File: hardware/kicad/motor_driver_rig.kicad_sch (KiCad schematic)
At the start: 8 parts, among them M1 NEMA-17 stepper motor, M2 NEMA-17 stepper motor, M3 NEMA-17 stepper motor, U1 Arduino Uno + CNC Shield V3

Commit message: schematics: name controller pins the way the boards name them
The three KiCad schematics labelled every controller pin by its MCU function
or STM32 port -- SCK, MISO, I2S_CLK, LED_DIN, PB0 -- which is not what any of
these boards is silkscreened with and not what you plug a wire into. Someone
holding an UNO Q and the schematic had no way to find "I2S_CLK".

Pins now carry the board's own header labels: D13/D12/D11/D8/D9/SCL/D10/A4/D3
on the UNO Q, D0-D10 on the XIAO, D2-D8 on the Uno under the CNC shield. The
signal's role moves into the net label, where it was already half-living
(SPI_SCK_D13, MIC_SD_A4), so each sensor stub still says both what the line
carries and which header pin it lands on. Sensor and driver symbols keep
their datasheet names -- those breakouts really are marked SCK/SDO/STEP.

Two labels were also just wrong, not merely inconvenient: the ring's DIN read
LED_DIN_PB0 when PB0 is header pin D3, and the mic's three lines read
PB10/PB9/PC1 with no header pin at all -- they are SCL, D10 and A4. Mapping is
the board's own gpio-map (arduino_r3_connector.dtsi) for the UNO Q and
board_pins.h for the XIAO; the mic's bit clock is genuinely the odd one out,
since PB10 comes out as the dedicated SCL pin rather than a D-number.

Appendix B.1's table gains the same treatment, and the report PNGs are
re-cropped to the drawing rather than the sheet -- they were carrying about
half a page of blank paper each, which shrank the schematic on the page. The
crop is now derived in the README instead of living in shell history.

Co-Authored-By: Claude Opus 5 <noreply@anthropic.com>
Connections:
- net EN renamed ENABLE_D8
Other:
- note added: "Arduino Uno + CNC Shield V3, one driver socket per motor axis. Shared ~ENABLE line on D8, active-LOW. Uno pins named by header number."
- note removed: "Arduino Uno + CNC Shield V3, one driver socket per motor axis. Shared ~ENABLE line, active-LOW."
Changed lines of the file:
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@@
 		(stroke (width 0) (type default))
 	)
-	(label "EN"
+	(label "ENABLE_D8"
 		(at 94.29 77.775 0)
 		(effects (font (size 1.27 1.27)) (justify left))
@@
 		(effects (font (size 1.27 1.27)) (justify right))
 	)
-	(label "EN"
+	(label "ENABLE_D8"
 		(at 147.06 73.175 0)
 		(effects (font (size 1.27 1.27)) (justify right))
@@
 		(effects (font (size 1.27 1.27)) (justify right))
 	)
-	(label "EN"
+	(label "ENABLE_D8"
 		(at 147.06 128.175 0)
 		(effects (font (size 1.27 1.27)) (justify right))
@@
 		(effects (font (size 1.27 1.27)) (justify right))
 	)
-	(label "EN"
+	(label "ENABLE_D8"
 		(at 147.06 183.175 0)
 		(effects (font (size 1.27 1.27)) (justify right))
@@
 		(effects (font (size 3.0 3.0)) (justify left))
 	)
-	(text "Arduino Uno + CNC Shield V3, one driver socket per motor axis. Shared ~ENABLE line, active-LOW."
+	(text "Arduino Uno + CNC Shield V3, one driver socket per motor axis. Shared ~ENABLE line on D8, active-LOW. Uno pins named by header number."
 		(exclude_from_sim no)
 		(at 20 32 0)
@@
 		(instances
 			(project "epm"
-				(path "/50f33c9c-fe69-4cc4-b722-142f8d680243"
+				(path "/2d634057-a69e-4741-94ac-d6e266f9f302"
 					(reference "U1")
 					(unit 1)
@@
 		(on_board yes)
 		(dnp no)
-		(property "Reference" "#PWR58db"
+		(property "Reference" "#PWRcf7e"
 			(at 94.29 118.41499999999999 0)
 			(effects (font (size 1.27 1.27)) (hide yes))
@@
 		(instances
 			(project "epm"
-				(path "/50f33c9c-fe69-4cc4-b722-142f8d680243"
-					(reference "#PWR58db")
+				(path "/2d634057-a69e-4741-94ac-d6e266f9f302"
+					(reference "#PWRcf7e")
 					(unit 1)
 				)
@@
 		(instances
 			(project "epm"
-				(path "/50f33c9c-fe69-4cc4-b722-142f8d680243"
+				(path "/2d634057-a69e-4741-94ac-d6e266f9f302"
 					(reference "A1")
 					(unit 1)
@@
 		(on_board yes)
 		(dnp no)
-		(property "Reference" "#PWR8cc8"
+		(property "Reference" "#PWRf5da"
 			(at 147.06 75.715 0)
 			(effects (font (size 1.27 1.27)) (hide yes))
@@
 		(instances
 			(project "epm"
-				(path "/50f33c9c-fe69-4cc4-b722-142f8d680243"
-					(reference "#PWR8cc8")
+				(path "/2d634057-a69e-4741-94ac-d6e266f9f302"
+					(reference "#PWRf5da")
 					(unit 1)
 				)
@@
 		(instances
 			(project "epm"
-				(path "/50f33c9c-fe69-4cc4-b722-142f8d680243"
+				(path "/2d634057-a69e-4741-94ac-d6e266f9f302"
 					(reference "M1")
 					(unit 1)
@@
 		(instances
 			(project "epm"
-				(path "/50f33c9c-fe69-4cc4-b722-142f8d680243"
+				(path "/2d634057-a69e-4741-94ac-d6e266f9f302"
 					(reference "A2")
 					(unit 1)
@@
 		(on_board yes)
 		(dnp no)
-		(property "Reference" "#PWRab13"
+		(property "Reference" "#PWRdf3b"
 			(at 147.06 130.715 0)
 			(effects (font (size 1.27 1.27)) (hide yes))
@@
 		(instances
 			(project "epm"
-				(path "/50f33c9c-fe69-4cc4-b722-142f8d680243"
-					(reference "#PWRab13")
+				(path "/2d634057-a69e-4741-94ac-d6e266f9f302"
+					(reference "#PWRdf3b")
 					(unit 1)
 				)
@@
 		(instances
 			(project "epm"
-				(path "/50f33c9c-fe69-4cc4-b722-142f8d680243"
+				(path "/2d634057-a69e-4741-94ac-d6e266f9f302"
 					(reference "M2")
 					(unit 1)
@@
 		(instances
 			(project "epm"
-				(path "/50f33c9c-fe69-4cc4-b722-142f8d680243"
+				(path "/2d634057-a69e-4741-94ac-d6e266f9f302"
 					(reference "A3")
 					(unit 1)
@@
 		(on_board yes)
 		(dnp no)
-		(property "Reference" "#PWR1313"
+		(property "Reference" "#PWRdb6c"
 			(at 147.06 185.715 0)
 			(effects (font (size 1.27 1.27)) (hide yes))
@@
 		(instances
 			(project "epm"
-				(path "/50f33c9c-fe69-4cc4-b722-142f8d680243"
-					(reference "#PWR1313")
+				(path "/2d634057-a69e-4741-94ac-d6e266f9f302"
+					(reference "#PWRdb6c")
 					(unit 1)
 				)
@@
 		(instances
 			(project "epm"
-				(path "/50f33c9c-fe69-4cc4-b722-142f8d680243"
+				(path "/2d634057-a69e-4741-94ac-d6e266f9f302"
 					(reference "M3")
 					(unit 1)
@@
 		(instances
 			(project "epm"
-				(path "/50f33c9c-fe69-4cc4-b722-142f8d680243"
+				(path "/2d634057-a69e-4741-94ac-d6e266f9f302"
 					(reference "PS1")
 					(unit 1)
@@
 		(on_board yes)
 		(dnp no)
-		(property "Reference" "#PWR4700"
+		(property "Reference" "#PWR7c5e"
 			(at 84.13 209.365 0)
 			(effects (font (size 1.27 1.27)) (hide yes))
@@
 		(instances
 			(project "epm"
-				(path "/50f33c9c-fe69-4cc4-b722-142f8d680243"
-					(reference "#PWR4700")
-					(unit 1)
-				)
+				(path "/2d634057-a69e-4741-94ac-d6e266f9f302"
+					(reference "#PWR7c5e")
+					(unit 1)
+				)

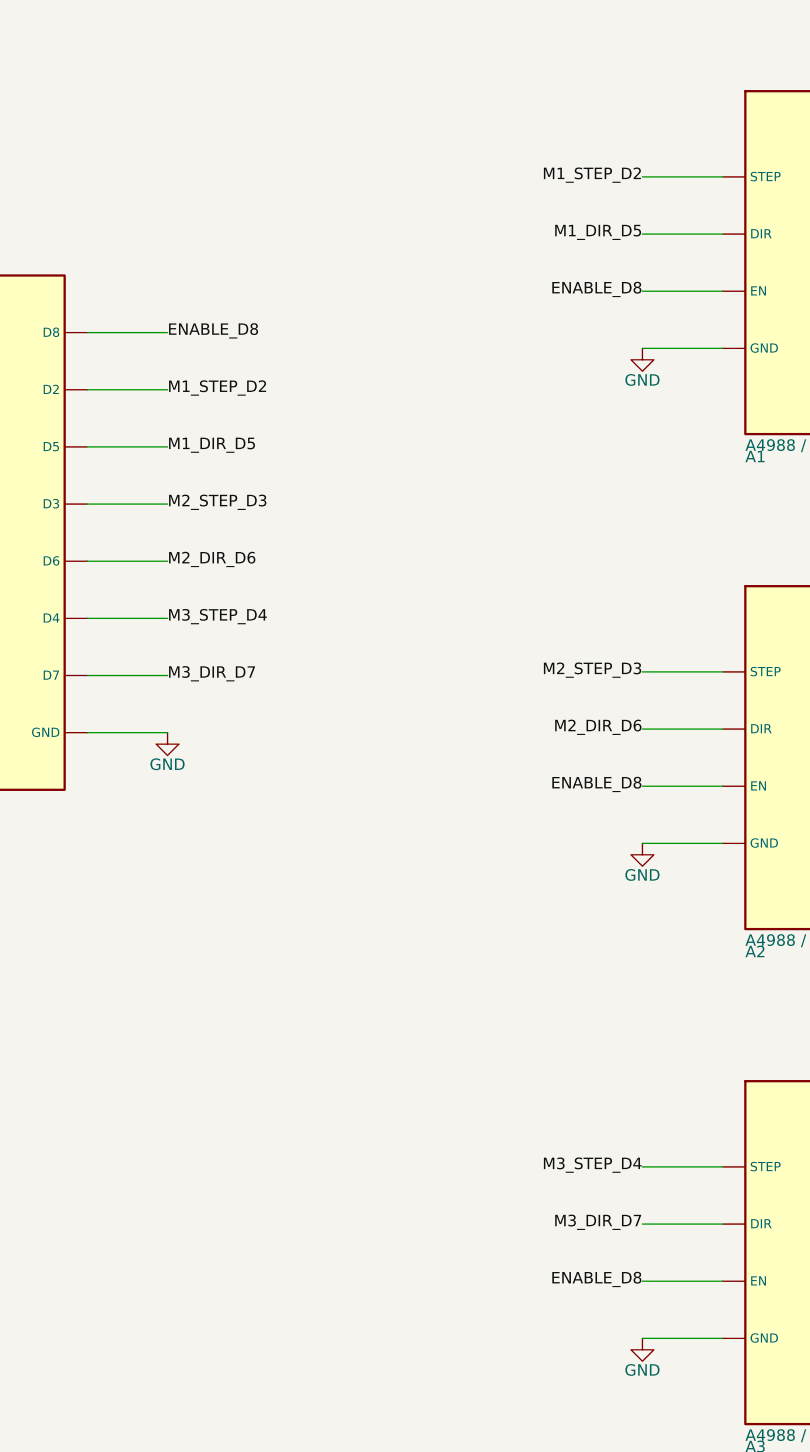
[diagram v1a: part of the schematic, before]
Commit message: schematics: drop redundant pin-number suffix from net labels
The symbol pin already shows the pin number (D8, A4, SCL, ...), so
repeating it in the net label (SPI_SCK_D8) was noise. Net labels now
carry only the signal role (SPI_SCK, MIC_SD, ENABLE, ...).

Co-Authored-By: Claude Sonnet 5 <noreply@anthropic.com>
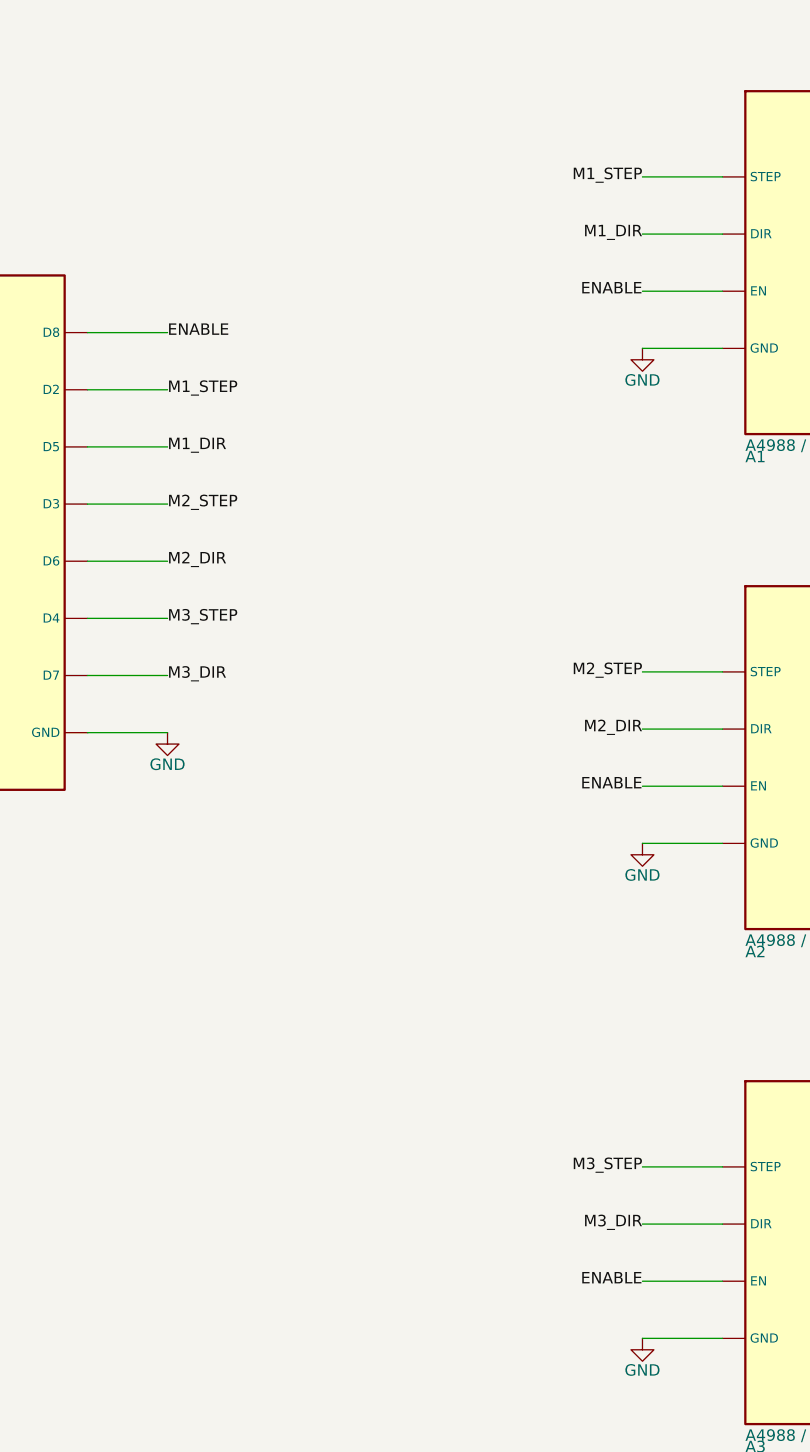
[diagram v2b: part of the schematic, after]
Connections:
- net ENABLE_D8 renamed ENABLE
- net M1_DIR_D5 renamed M1_DIR
- net M1_STEP_D2 renamed M1_STEP
- net M2_DIR_D6 renamed M2_DIR
- net M2_STEP_D3 renamed M2_STEP
- net M3_DIR_D7 renamed M3_DIR
- net M3_STEP_D4 renamed M3_STEP
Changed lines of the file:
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@@
 		(stroke (width 0) (type default))
 	)
-	(label "ENABLE_D8"
+	(label "ENABLE"
 		(at 94.29 77.775 0)
 		(effects (font (size 1.27 1.27)) (justify left))
 	)
-	(label "M1_STEP_D2"
+	(label "M1_STEP"
 		(at 94.29 84.125 0)
 		(effects (font (size 1.27 1.27)) (justify left))
 	)
-	(label "M1_DIR_D5"
+	(label "M1_DIR"
 		(at 94.29 90.475 0)
 		(effects (font (size 1.27 1.27)) (justify left))
 	)
-	(label "M2_STEP_D3"
+	(label "M2_STEP"
 		(at 94.29 96.825 0)
 		(effects (font (size 1.27 1.27)) (justify left))
 	)
-	(label "M2_DIR_D6"
+	(label "M2_DIR"
 		(at 94.29 103.175 0)
 		(effects (font (size 1.27 1.27)) (justify left))
 	)
-	(label "M3_STEP_D4"
+	(label "M3_STEP"
 		(at 94.29 109.525 0)
 		(effects (font (size 1.27 1.27)) (justify left))
 	)
-	(label "M3_DIR_D7"
+	(label "M3_DIR"
 		(at 94.29 115.875 0)
 		(effects (font (size 1.27 1.27)) (justify left))
 	)
-	(label "M1_STEP_D2"
+	(label "M1_STEP"
 		(at 147.06 60.475 0)
 		(effects (font (size 1.27 1.27)) (justify right))
 	)
-	(label "M1_DIR_D5"
+	(label "M1_DIR"
 		(at 147.06 66.825 0)
 		(effects (font (size 1.27 1.27)) (justify right))
 	)
-	(label "ENABLE_D8"
+	(label "ENABLE"
 		(at 147.06 73.175 0)
 		(effects (font (size 1.27 1.27)) (justify right))
@@
 		(effects (font (size 1.27 1.27)) (justify right))
 	)
-	(label "M2_STEP_D3"
+	(label "M2_STEP"
 		(at 147.06 115.475 0)
 		(effects (font (size 1.27 1.27)) (justify right))
 	)
-	(label "M2_DIR_D6"
+	(label "M2_DIR"
 		(at 147.06 121.825 0)
 		(effects (font (size 1.27 1.27)) (justify right))
 	)
-	(label "ENABLE_D8"
+	(label "ENABLE"
 		(at 147.06 128.175 0)
 		(effects (font (size 1.27 1.27)) (justify right))
@@
 		(effects (font (size 1.27 1.27)) (justify right))
 	)
-	(label "M3_STEP_D4"
+	(label "M3_STEP"
 		(at 147.06 170.475 0)
 		(effects (font (size 1.27 1.27)) (justify right))
 	)
-	(label "M3_DIR_D7"
+	(label "M3_DIR"
 		(at 147.06 176.825 0)
 		(effects (font (size 1.27 1.27)) (justify right))
 	)
-	(label "ENABLE_D8"
+	(label "ENABLE"
 		(at 147.06 183.175 0)
 		(effects (font (size 1.27 1.27)) (justify right))
@@
 		(instances
 			(project "epm"
-				(path "/2d634057-a69e-4741-94ac-d6e266f9f302"
+				(path "/87b9f554-06cc-464e-9778-1c1825e64535"
 					(reference "U1")
 					(unit 1)
@@
 		(on_board yes)
 		(dnp no)
-		(property "Reference" "#PWRcf7e"
+		(property "Reference" "#PWRf291"
 			(at 94.29 118.41499999999999 0)
 			(effects (font (size 1.27 1.27)) (hide yes))
@@
 		(instances
 			(project "epm"
-				(path "/2d634057-a69e-4741-94ac-d6e266f9f302"
-					(reference "#PWRcf7e")
+				(path "/87b9f554-06cc-464e-9778-1c1825e64535"
+					(reference "#PWRf291")
 					(unit 1)
 				)
@@
 		(instances
 			(project "epm"
-				(path "/2d634057-a69e-4741-94ac-d6e266f9f302"
+				(path "/87b9f554-06cc-464e-9778-1c1825e64535"
 					(reference "A1")
 					(unit 1)
@@
 		(on_board yes)
 		(dnp no)
-		(property "Reference" "#PWRf5da"
+		(property "Reference" "#PWRebbc"
 			(at 147.06 75.715 0)
 			(effects (font (size 1.27 1.27)) (hide yes))
@@
 		(instances
 			(project "epm"
-				(path "/2d634057-a69e-4741-94ac-d6e266f9f302"
-					(reference "#PWRf5da")
+				(path "/87b9f554-06cc-464e-9778-1c1825e64535"
+					(reference "#PWRebbc")
 					(unit 1)
 				)
@@
 		(instances
 			(project "epm"
-				(path "/2d634057-a69e-4741-94ac-d6e266f9f302"
+				(path "/87b9f554-06cc-464e-9778-1c1825e64535"
 					(reference "M1")
 					(unit 1)
@@
 		(instances
 			(project "epm"
-				(path "/2d634057-a69e-4741-94ac-d6e266f9f302"
+				(path "/87b9f554-06cc-464e-9778-1c1825e64535"
 					(reference "A2")
 					(unit 1)
@@
 		(on_board yes)
 		(dnp no)
-		(property "Reference" "#PWRdf3b"
+		(property "Reference" "#PWR8031"
 			(at 147.06 130.715 0)
 			(effects (font (size 1.27 1.27)) (hide yes))
@@
 		(instances
 			(project "epm"
-				(path "/2d634057-a69e-4741-94ac-d6e266f9f302"
-					(reference "#PWRdf3b")
+				(path "/87b9f554-06cc-464e-9778-1c1825e64535"
+					(reference "#PWR8031")
 					(unit 1)
 				)
@@
 		(instances
 			(project "epm"
-				(path "/2d634057-a69e-4741-94ac-d6e266f9f302"
+				(path "/87b9f554-06cc-464e-9778-1c1825e64535"
 					(reference "M2")
 					(unit 1)
@@
 		(instances
 			(project "epm"
-				(path "/2d634057-a69e-4741-94ac-d6e266f9f302"
+				(path "/87b9f554-06cc-464e-9778-1c1825e64535"
 					(reference "A3")
 					(unit 1)
@@
 		(on_board yes)
 		(dnp no)
-		(property "Reference" "#PWRdb6c"
+		(property "Reference" "#PWR5ca7"
 			(at 147.06 185.715 0)
 			(effects (font (size 1.27 1.27)) (hide yes))
@@
 		(instances
 			(project "epm"
-				(path "/2d634057-a69e-4741-94ac-d6e266f9f302"
-					(reference "#PWRdb6c")
+				(path "/87b9f554-06cc-464e-9778-1c1825e64535"
+					(reference "#PWR5ca7")
 					(unit 1)
 				)
@@
 		(instances
 			(project "epm"
-				(path "/2d634057-a69e-4741-94ac-d6e266f9f302"
+				(path "/87b9f554-06cc-464e-9778-1c1825e64535"
 					(reference "M3")
 					(unit 1)
@@
 		(instances
 			(project "epm"
-				(path "/2d634057-a69e-4741-94ac-d6e266f9f302"
+				(path "/87b9f554-06cc-464e-9778-1c1825e64535"
 					(reference "PS1")
 					(unit 1)
@@
 		(on_board yes)
 		(dnp no)
-		(property "Reference" "#PWR7c5e"
+		(property "Reference" "#PWR22c7"
 			(at 84.13 209.365 0)
 			(effects (font (size 1.27 1.27)) (hide yes))
@@
 		(instances
 			(project "epm"
-				(path "/2d634057-a69e-4741-94ac-d6e266f9f302"
-					(reference "#PWR7c5e")
-					(unit 1)
-				)
+				(path "/87b9f554-06cc-464e-9778-1c1825e64535"
+					(reference "#PWR22c7")
+					(unit 1)
+				)
